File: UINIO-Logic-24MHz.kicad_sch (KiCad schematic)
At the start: 51 parts, among them J1 Conn_01x10_Pin, U1 AT24CS64-XHM, U2 74HC245C, U3 ME6211C33M5G-N, U4 CY7C68013A-56LTX, Y1 24MHz

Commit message: update hardware
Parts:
- removed F1: 60V 1A, Fuse:Fuse_1206_3216Metric, symbol Device:Fuse
- removed J1: Conn_01x10_Pin, Connector_PinHeader_2.54mm:PinHeader_1x10_P2.54mm_Vertical, symbol Connector:Conn_01x10_Pin
- removed U3: ME6211C33M5G-N, Uinio:SOT-23-5_L3.0-W1.7-P0.95-LS2.8-BR, symbol Uinio:ME6211
- removed Y1: 24MHz, Crystal:Crystal_SMD_3225-4Pin_3.2x2.5mm, symbol Device:Crystal_GND24
- added J1: DE9_Pins, symbol Connector:DE9_Pins
- added J2: Conn_02x05_Odd_Even, symbol Connector_Generic:Conn_02x05_Odd_Even
- added U3: AP2127N-3.3, Package_TO_SOT_SMD:SOT-23, symbol Regulator_Linear:AP2127N-3.3
- added Y2: Crystal, Crystal:Crystal_SMD_HC49-SD, symbol Device:Crystal
- U1: footprint Package_SO:TSSOP-8_4.4x3mm_P0.65mm -> Package_SO:SO-8_3.9x4.9mm_P1.27mm
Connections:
- net +3.3V: now also C2.2, U3.2 (VO)
- net +5V: now also U3.3 (VI)
- net GND: now also J2.10 (Pin_10), J2.9 (Pin_9), U3.1 (GND)
- net D5: now reaches R4.2
- net D5: now also J2.5 (Pin_5)
- net at C9.2, U4.5 (XTALIN): now also Y2.1
- net D7: now reaches R2.2
- net D7: now also J2.7 (Pin_7)
- net at C8.2, U4.4 (XTALOUT): now also Y2.2
- net D4: now reaches R5.2
- net D4: now also J2.4 (Pin_4)
- net D6: now reaches R3.2
- net D6: now also J2.6 (Pin_6)
- net D3: now reaches R6.2
- net D3: now also J2.3 (Pin_3)
- net D1: now reaches R8.2
- net D1: now also J2.1 (Pin_1)
- net D2: now reaches R7.2
- net D2: now also J2.2 (Pin_2)
- net D8: now reaches R1.2
- net D8: now also J2.8 (Pin_8)
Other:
- note added: "EEPROM"
- note removed: "EEPROM 存储器"
- note removed: "信 号 收 发 器"
- moved on the sheet: C1

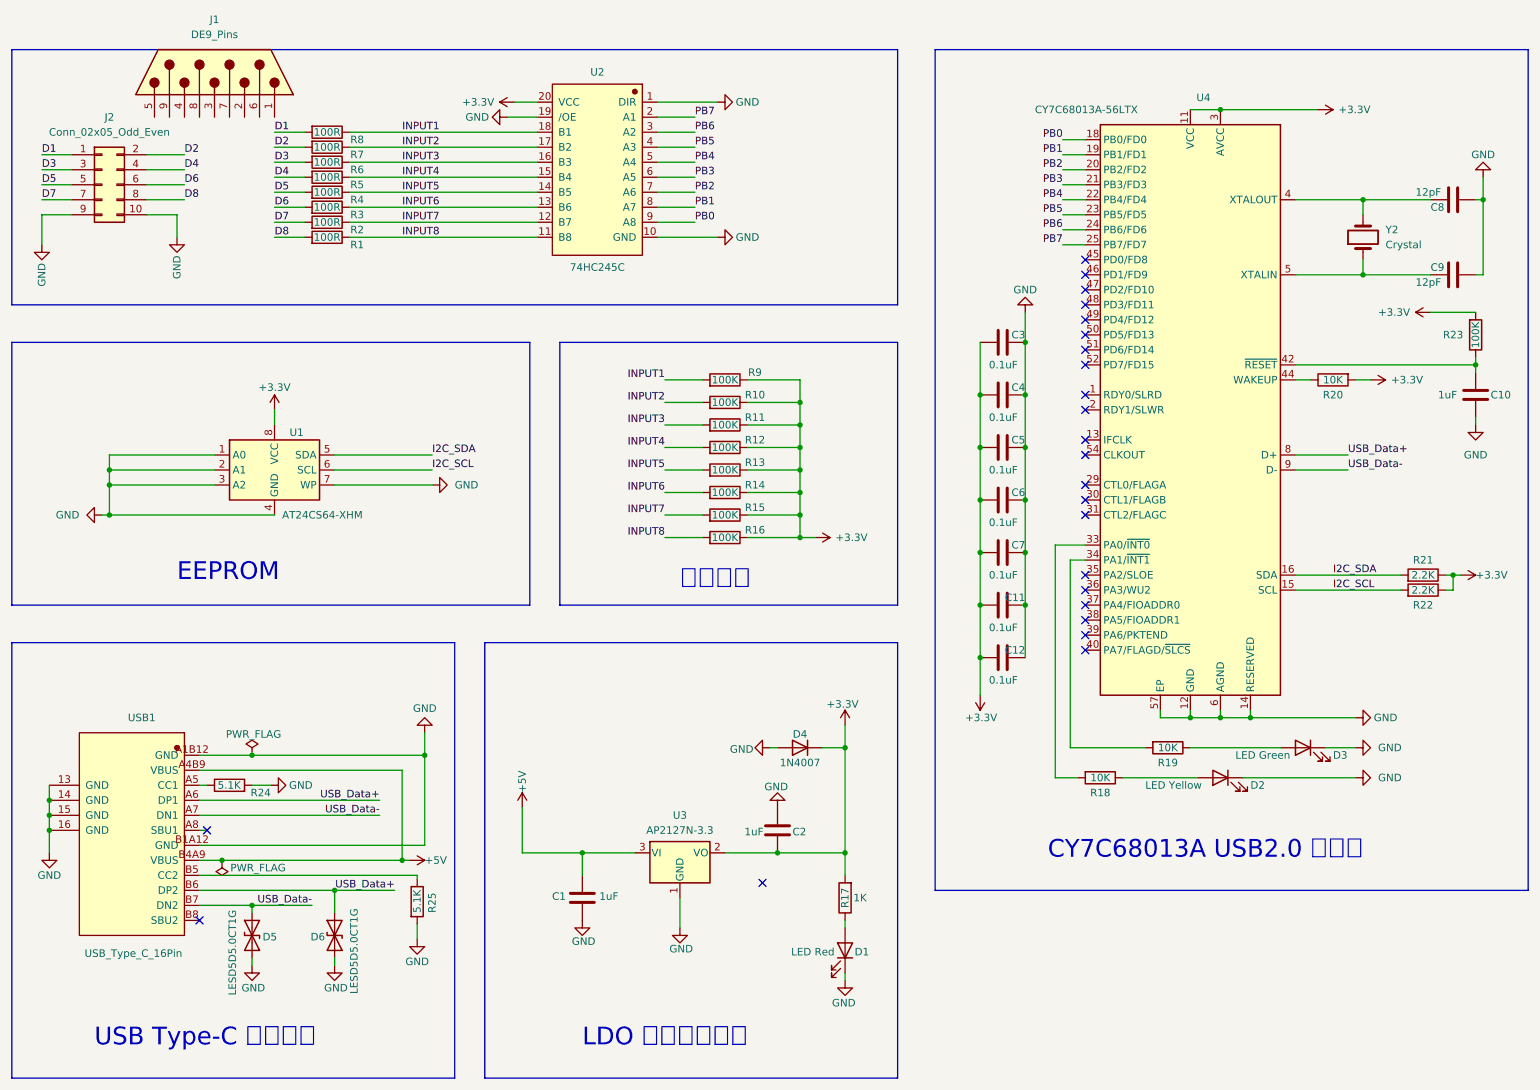
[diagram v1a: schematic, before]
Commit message: update sch & brd with saleae clone hardware
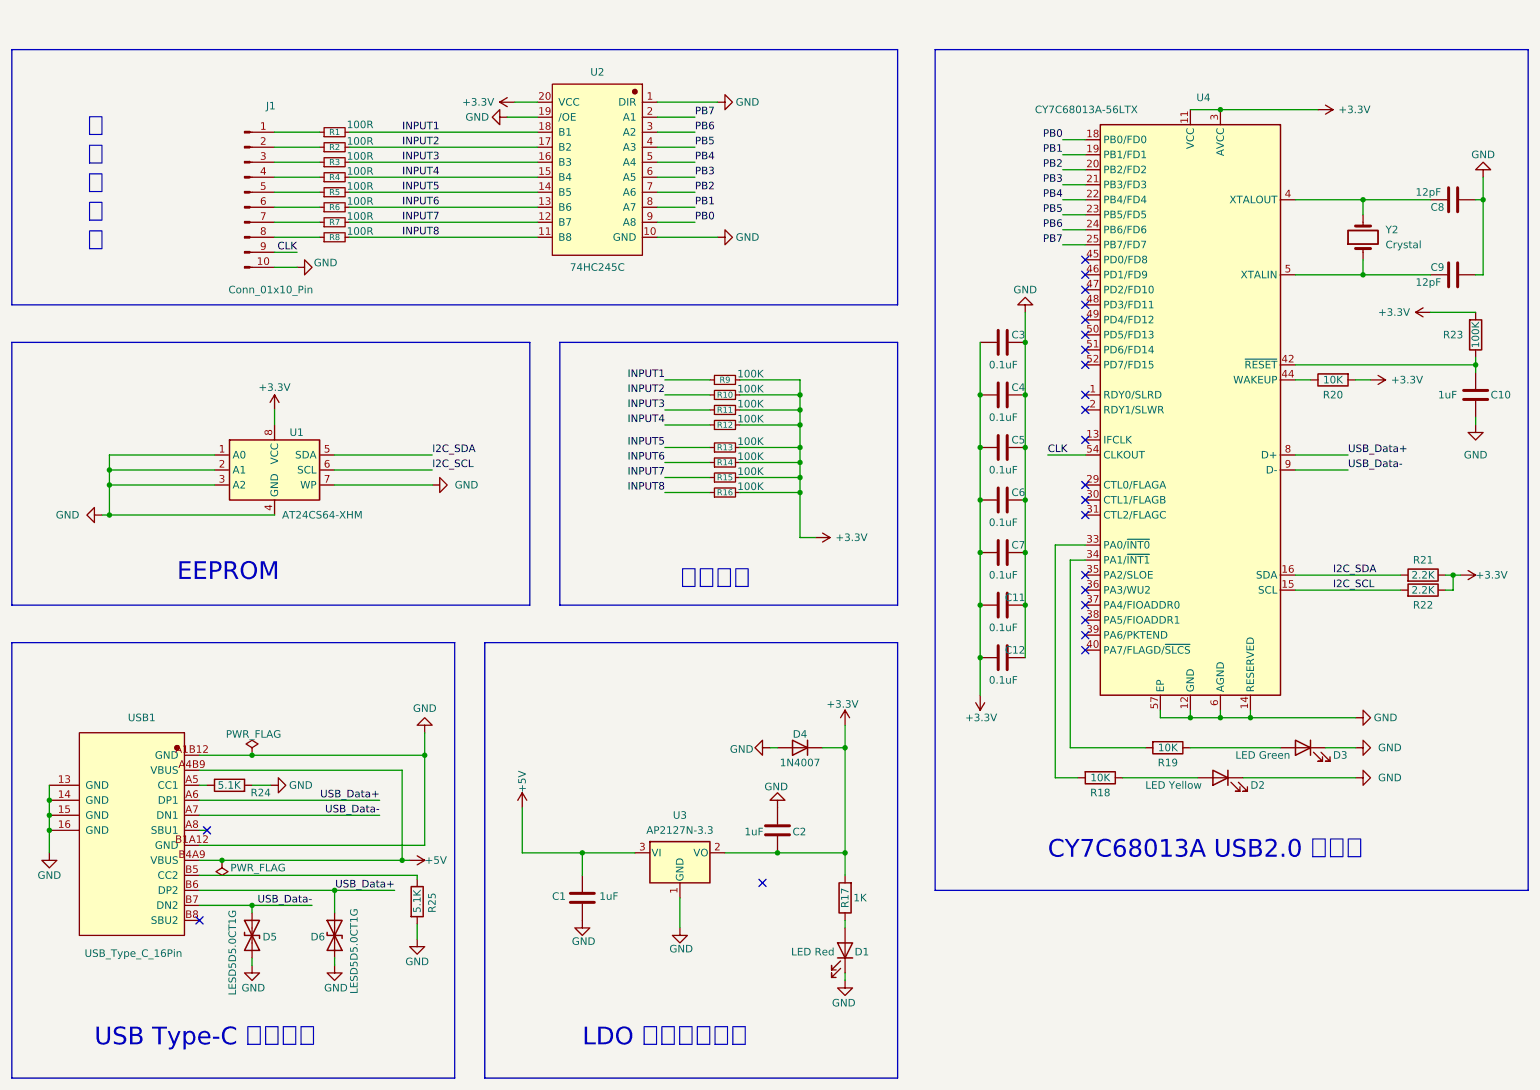
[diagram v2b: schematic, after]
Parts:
- removed J1: DE9_Pins, symbol Connector:DE9_Pins
- removed J2: Conn_02x05_Odd_Even, symbol Connector_Generic:Conn_02x05_Odd_Even
- removed R1, R2, R3, R4, R5, R6, R7, R8: 100R, Resistor_SMD:R_0402_1005Metric, symbol Device:R
- removed R10, R11, R12, R13, R14, R15, R16, R9: 100K, Resistor_SMD:R_0402_1005Metric, symbol Device:R
- added J1: Conn_01x10_Pin, Uinio:IDC-Header_2x05_P2.54mm_EdgeMount, symbol Connector:Conn_01x10_Pin
- added R1, R2, R3, R4, R5, R6, R7, R8: 100R, Resistor_SMD:R_0603_1608Metric, symbol Device:R_Small
- added R10, R11, R12, R13, R14, R15, R16, R9: 100K, Resistor_SMD:R_0603_1608Metric, symbol Device:R_Small
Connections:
- net +3.3V: now also R10.2, R11.2, R12.2, R13.2, R14.2, R15.2, R16.2, R9.2
- net GND: now also J1.10 (Pin_10)
- net INPUT1: now also R1.2, R9.1
- net INPUT2: now also R10.1, R2.2
- net INPUT3: now also R11.1, R3.2
- net INPUT4: now also R12.1, R4.2
- net INPUT5: now also R13.1, R5.2
- net INPUT6: now also R14.1, R6.2
- net INPUT7: now also R15.1, R7.2
- net INPUT8: now also R16.1, R8.2
- net CLK: now reaches U4.54 (CLKOUT)
- net CLK: now also J1.9 (Pin_9)
- new net: J1.2 (Pin_2), R2.1
- new net: J1.3 (Pin_3), R3.1
- new net: J1.4 (Pin_4), R4.1
- new net: J1.8 (Pin_8), R8.1
- new net: J1.6 (Pin_6), R6.1
- new net: J1.1 (Pin_1), R1.1
- new net: J1.5 (Pin_5), R5.1
- new net: J1.7 (Pin_7), R7.1
- no-connect marks 24 -> 23
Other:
- note added: "信 号 收 发 器"

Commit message: fix some routing
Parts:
- removed C12: 0.1uF, Capacitor_SMD:C_0402_1005Metric, symbol Device:C
- removed D4: 1N4007, Diode_SMD:Nexperia_CFP3_SOD-123W, symbol Diode:1N4007
- added JP1, JP2, JP3, JP4, JP5, JP6, JP7, JP8: (no value), Uinio:SolderJumper-2_Open_RoundedPad_small, symbol Jumper:Jumper_2_Small_Open
- added JP10, JP9: (no value), Uinio:SolderJumper-2_Bridged2Bar_RoundedPad_small, symbol Jumper:Jumper_2_Small_Bridged
- C10, C11, C3, C4, C5, C6, C7, C8, C9: footprint Capacitor_SMD:C_0402_1005Metric -> Capacitor_SMD:C_0603_1608Metric
- D1, D2, D3: footprint LED_SMD:LED_0603_1608Metric -> LED_SMD:LED_0805_2012Metric
- R17, R18, R19, R20, R21, R22, R23: footprint Resistor_SMD:R_0402_1005Metric -> Resistor_SMD:R_0603_1608Metric
- U4: footprint Package_DFN_QFN:QFN-56-1EP_8x8mm_P0.5mm_EP4.5x5.2mm_ThermalVias_TopTented -> Package_DFN_QFN:QFN-56-1EP_8x8mm_P0.5mm_EP4.5x5.2mm_ThermalVias
- USB1: footprint Uinio:USB-C-SMD_TYPEC-304J-BCP16 -> Connector_USB:USB_C_Receptacle_GCT_USB4105-xx-A_16P_TopMnt_Horizontal
- Y2: footprint Crystal:Crystal_SMD_HC49-SD -> Crystal:Crystal_HC49-4H_Vertical
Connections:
- net I2C_SCL: now also JP10.2 (B); no longer R22.2, U1.6 (SCL)
- net I2C_SDA: now also JP9.2 (B); no longer R21.2, U1.5 (SDA)
- net INPUT1: now also JP1.2 (B)
- net INPUT2: now also JP2.2 (B)
- net INPUT3: now also JP3.2 (B)
- net INPUT4: now also JP4.2 (B)
- net INPUT5: now also JP5.2 (B)
- net INPUT6: now also JP6.2 (B)
- net INPUT7: now also JP7.2 (B)
- net INPUT8: now also JP8.2 (B)
- net PB0: now also U2.2 (A1), JP1.1 (A); no longer U2.9 (A8)
- net PB1: now also U2.3 (A2), JP2.1 (A); no longer U2.8 (A7)
- net PB2: now also U2.4 (A3), JP3.1 (A); no longer U2.7 (A6)
- net PB3: now also U2.5 (A4), JP4.1 (A); no longer U2.6 (A5)
- net PB4: now also U2.6 (A5), JP5.1 (A); no longer U2.5 (A4)
- net PB5: now also U2.7 (A6), JP6.1 (A); no longer U2.4 (A3)
- net PB6: now also U2.8 (A7), JP7.1 (A); no longer U2.3 (A2)
- net PB7: now also U2.9 (A8), JP8.1 (A); no longer U2.2 (A1)
- new net: JP9.1 (A), R22.2, U1.5 (SDA)
- new net: JP10.1 (A), R21.2, U1.6 (SCL)
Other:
- note added: "LDO"
- note added: "USB Type-C"
- note removed: "LDO 线性稳压电路"
- note removed: "USB Type-C 接口电路"
- note removed: "信 号 收 发 器"
- moved on the sheet: J1, R1, R2, R21, R22, R3, R4, R5, R6, R7, R8, U2

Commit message: update routing
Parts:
- USB1: footprint Connector_USB:USB_C_Receptacle_GCT_USB4105-xx-A_16P_TopMnt_Horizontal -> Uinio:USB-C-SMD_TYPEC-304J-BCP16
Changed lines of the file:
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@@
 			)
 		)
-		(property "Footprint" "Connector_USB:USB_C_Receptacle_GCT_USB4105-xx-A_16P_TopMnt_Horizontal"
+		(property "Footprint" "Uinio:USB-C-SMD_TYPEC-304J-BCP16"
 			(at 40.64 135.89 0)
 			(hide yes)
